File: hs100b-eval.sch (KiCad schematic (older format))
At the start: 42 parts, among them IC1 HS-100B, J1 SPKR, J2 MIC, J3 RADIO_DATA, SW1 MUTE_REC, SW2 MUTE_PLAY, SW3 VOL_DN, SW4 VOL_UP

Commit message: Swap Molex micro USB for CUI
The Molex is nearly impossible to hand solder
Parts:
- removed JP2: USB_A, Connector_USB:USB_Micro-B_Molex_47346-0001, symbol Connector:USB_A
- added JP2: USB_B_Micro, CUI:UJ2-MIBH-4-SMT, symbol Connector:USB_B_Micro
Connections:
- net GND: now also JP2.5 (GND)
- net at L1.1: now also JP2.1 (VBUS)
- net USB-: now reaches C3.1, R1.2
- net USB-: now also JP2.2 (D-)
- net USB+: now reaches C4.1, R2.2
- net USB+: now also JP2.3 (D+)
- net at L2.2: now also JP2.6 (Shield)
- no-connect marks 7 -> 8
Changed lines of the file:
@@
 Sheet 1 1
 Title "HS100B Evaluation Board"
-Date "2021-04-05"
-Rev "1"
+Date "2021-04-14"
+Rev "2"
 Comp "Chris Keller"
 Comment1 ""
@@
 	1    0    0    -1
 $EndComp
-$Comp
-L Connector:USB_A JP2
-U 1 1 6057963A
-P 1350 2850
-F 0 "JP2" H 1407 3317 50  0000 C CNN
-F 1 "USB_A" H 1407 3226 50  0000 C CNN
-F 2 "Connector_USB:USB_Micro-B_Molex_47346-0001" H 1500 2800 50  0001 C CNN
-F 3 "https://www.mouser.com/datasheet/2/276/0473460001_IO_CONNECTORS-229243.pdf" H 1500 2800 50  0001 C CNN
-F 4 "0.95" H 1407 3417 50  0001 C CNN "Price"
-F 5 "538-47346-0001" H 1407 3417 50  0001 C CNN "Vendor Part #"
-F 6 "Mouser" H 1407 3417 50  0001 C CNN "Vendor"
-	1    1350 2850
-	1    0    0    -1
-$EndComp
 Wire Wire Line
 	1350 3250 1350 3600
@@
 NoConn ~ 4050 4150
 NoConn ~ 4050 4350
+$Comp
+L Connector:USB_B_Micro JP2
+U 1 1 6078D129
+P 1350 2850
+F 0 "JP2" H 1407 3317 50  0000 C CNN
+F 1 "USB_B_Micro" H 1407 3226 50  0000 C CNN
+F 2 "CUI:UJ2-MIBH-4-SMT" H 1500 2800 50  0001 C CNN
+F 3 "https://www.mouser.com/datasheet/2/670/uj2_mibh_4_smt-1313358.pdf" H 1500 2800 50  0001 C CNN
+	1    1350 2850
+	1    0    0    -1
+$EndComp
+NoConn ~ 1650 3050
+Text Label 1750 2850 0    50   ~ 0
+USB+
+Text Label 1750 2950 0    50   ~ 0
+USB-
 $EndSCHEMATC

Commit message: Update BOM
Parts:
- IC1: Description LQFP-48 Video-Audio Interface ICs RoHS -> (none); Height 1.6 -> (none); Manufacturer_Name cmedia -> (none); Manufacturer_Part_Number HS-100B -> (none); Price (none) -> 0.78; Vendor (none) -> Symmetry; Vendor Part # (none) -> HS-100B
- JP2: Price (none) -> 0.79; Vendor (none) -> Mouser; Vendor Part # (none) -> 490-UJ2-MIBH-4-SMT
- R4: Vendor Part # 661-RK73Z2ETTD -> 660-RK73Z2ETTD
- R5: Vendor Part # 662-RK73Z2ETTD -> 660-RK73Z2ETTD
- R6: Vendor Part # 663-RK73Z2ETTD -> 660-RK73Z2ETTD

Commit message: Add more test points
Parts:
- added TP1: GND, TestPoint:TestPoint_Pad_D2.0mm, symbol Connector:TestPoint_Flag
- added TP2: 5V, TestPoint:TestPoint_Pad_D1.0mm, symbol Connector:TestPoint_Flag
- C50, C51: footprint 293D477X9010E2TE3:CAPPM7343X430N -> Vishay:CAPPM7343X430N
- TP3: renamed from TP1; value Test_3V3 -> 3V3
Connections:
- net GND: now also TP1.1
- net VBUS: now also TP2.1
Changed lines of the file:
@@
 $EndComp
 $Comp
-L Connector:TestPoint_Flag TP1
+L Connector:TestPoint_Flag TP3
 U 1 1 605AD28D
 P 3450 4250
-F 0 "TP1" V 3847 4298 50  0000 C CNN
-F 1 "Test_3V3" V 3756 4298 50  0000 C CNN
+F 0 "TP3" V 3847 4298 50  0000 C CNN
+F 1 "3V3" V 3756 4298 50  0000 C CNN
 F 2 "TestPoint:TestPoint_Pad_D1.0mm" H 3650 4250 50  0001 C CNN
 F 3 "-" H 3650 4250 50  0001 C CNN
@@
 F 0 "C50" V 6855 3950 50  0000 C CNN
 F 1 "470μF" V 6764 3950 50  0000 C CNN
-F 2 "293D477X9010E2TE3:CAPPM7343X430N" H 6638 3800 50  0001 C CNN
+F 2 "Vishay:CAPPM7343X430N" H 6638 3800 50  0001 C CNN
 F 3 "https://www.mouser.com/datasheet/2/427/293d-1763499.pdf" H 6600 3950 50  0001 C CNN
 F 4 "1.3" H 6855 4050 50  0001 C CNN "Price"
@@
 F 0 "C51" V 7150 4050 50  0000 C CNN
 F 1 "470μF" V 7050 4050 50  0000 C CNN
-F 2 "293D477X9010E2TE3:CAPPM7343X430N" H 6938 3900 50  0001 C CNN
+F 2 "Vishay:CAPPM7343X430N" H 6938 3900 50  0001 C CNN
 F 3 "https://www.mouser.com/datasheet/2/427/293d-1763499.pdf" H 6900 4050 50  0001 C CNN
 F 4 "1.3" H 7150 4150 50  0001 C CNN "Price"
@@
 	2050 2650 2150 2650
 Wire Wire Line
-	2150 2650 2150 2400
+	2150 2650 2150 2500
 Wire Wire Line
 	8900 5150 8700 5150
@@
 	2750 5300 2750 5800
 Wire Wire Line
-	1350 3250 1350 3600
+	1350 3250 1350 3550
 Wire Wire Line
 	1250 3250 1250 3300
@@
 	5050 5450 5150 5450
 Wire Wire Line
-	4950 5450 4950 5650
+	4950 5450 4950 5600
 Wire Wire Line
 	5750 4450 7000 4450
@@
 	6100 5100 6100 3700
 Wire Wire Line
-	7200 2300 7200 2600
+	7200 2300 7200 2450
 Wire Wire Line
 	5900 2600 5900 3400
@@
 NoConn ~ 4050 4350
 NoConn ~ 1650 3050
+$Comp
+L Connector:TestPoint_Flag TP2
+U 1 1 607D02CD
+P 7200 2450
+F 0 "TP2" V 7354 2590 50  0000 L CNN
+F 1 "5V" V 7263 2590 50  0000 L CNN
+F 2 "TestPoint:TestPoint_Pad_D1.0mm" H 7400 2450 50  0001 C CNN
+F 3 "-" H 7400 2450 50  0001 C CNN
+F 4 "0" H 7597 2598 50  0001 C CNN "Price"
+F 5 "-" H 7597 2598 50  0001 C CNN "Vendor Part #"
+F 6 "-" H 7597 2598 50  0001 C CNN "Vendor"
+	1    7200 2450
+	0    -1   -1   0
+$EndComp
+Connection ~ 2150 2500
+Wire Wire Line
+	2150 2500 2150 2400
+$Comp
+L Connector:TestPoint_Flag TP1
+U 1 1 607D1285
+P 4950 5600
+F 0 "TP1" H 5210 5694 50  0000 L CNN
+F 1 "GND" H 5210 5603 50  0000 L CNN
+F 2 "TestPoint:TestPoint_Pad_D2.0mm" H 5150 5600 50  0001 C CNN
+F 3 "-" H 5150 5600 50  0001 C CNN
+F 4 "0" H 5347 5748 50  0001 C CNN "Price"
+F 5 "-" H 5347 5748 50  0001 C CNN "Vendor Part #"
+F 6 "-" H 5347 5748 50  0001 C CNN "Vendor"
+	1    4950 5600
+	1    0    0    -1
+$EndComp
+Connection ~ 1350 3550
+Wire Wire Line
+	1350 3550 1350 3600
+Connection ~ 4950 5600
+Wire Wire Line
+	4950 5600 4950 5650
+Connection ~ 7200 2550
+Wire Wire Line
+	7200 2550 7200 2600
+Connection ~ 7200 2450
+Wire Wire Line
+	7200 2450 7200 2550
 $EndSCHEMATC

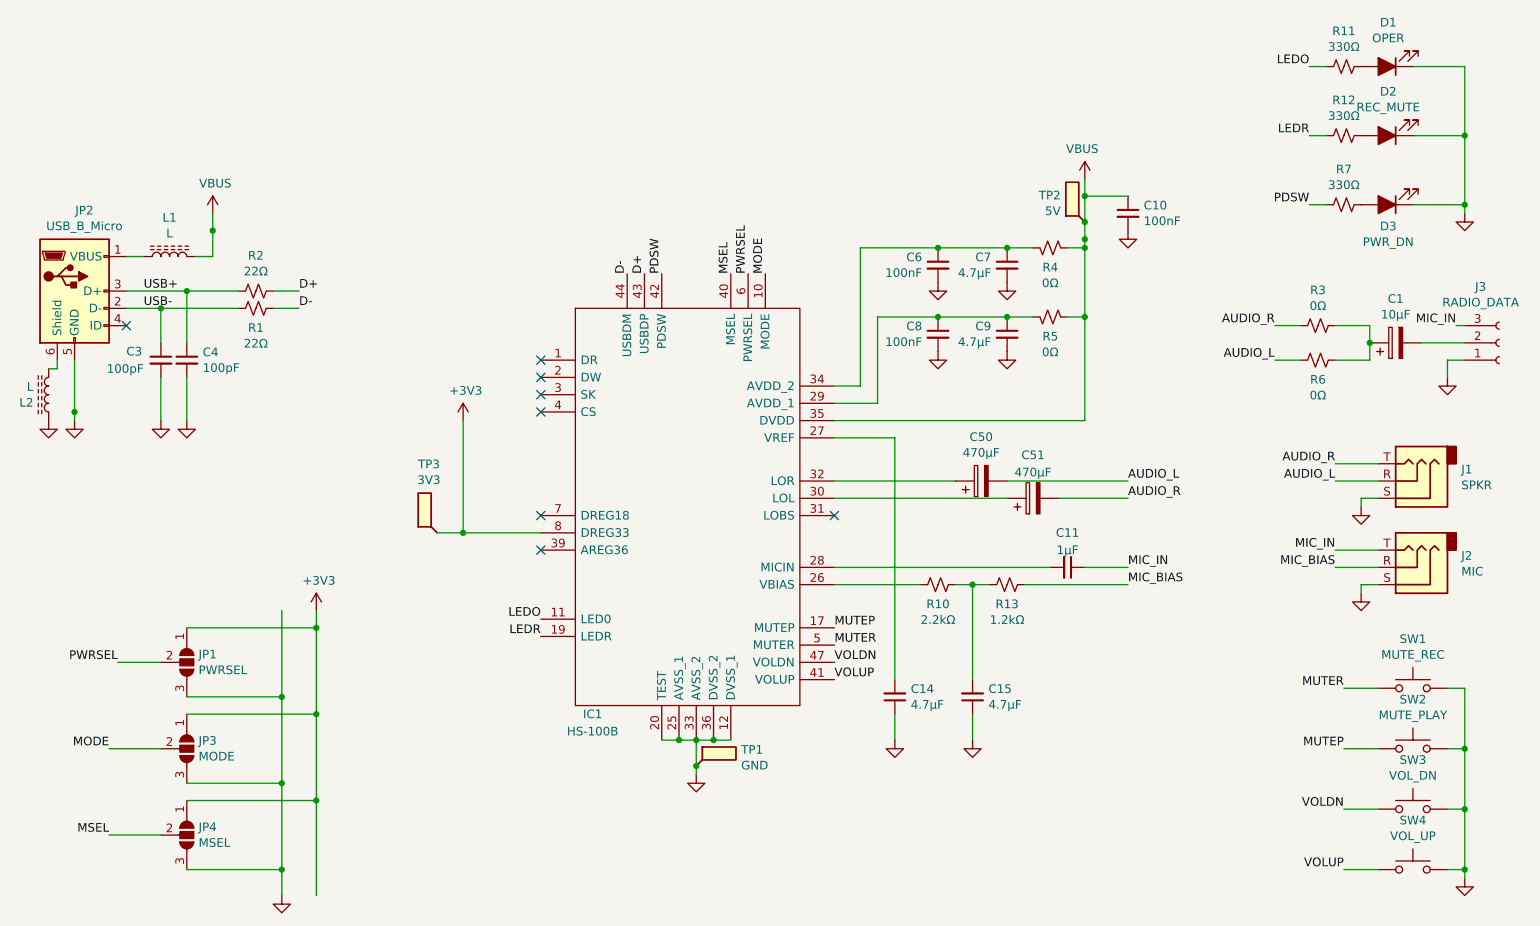
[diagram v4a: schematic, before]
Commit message: Move 5V test point to directly off USB
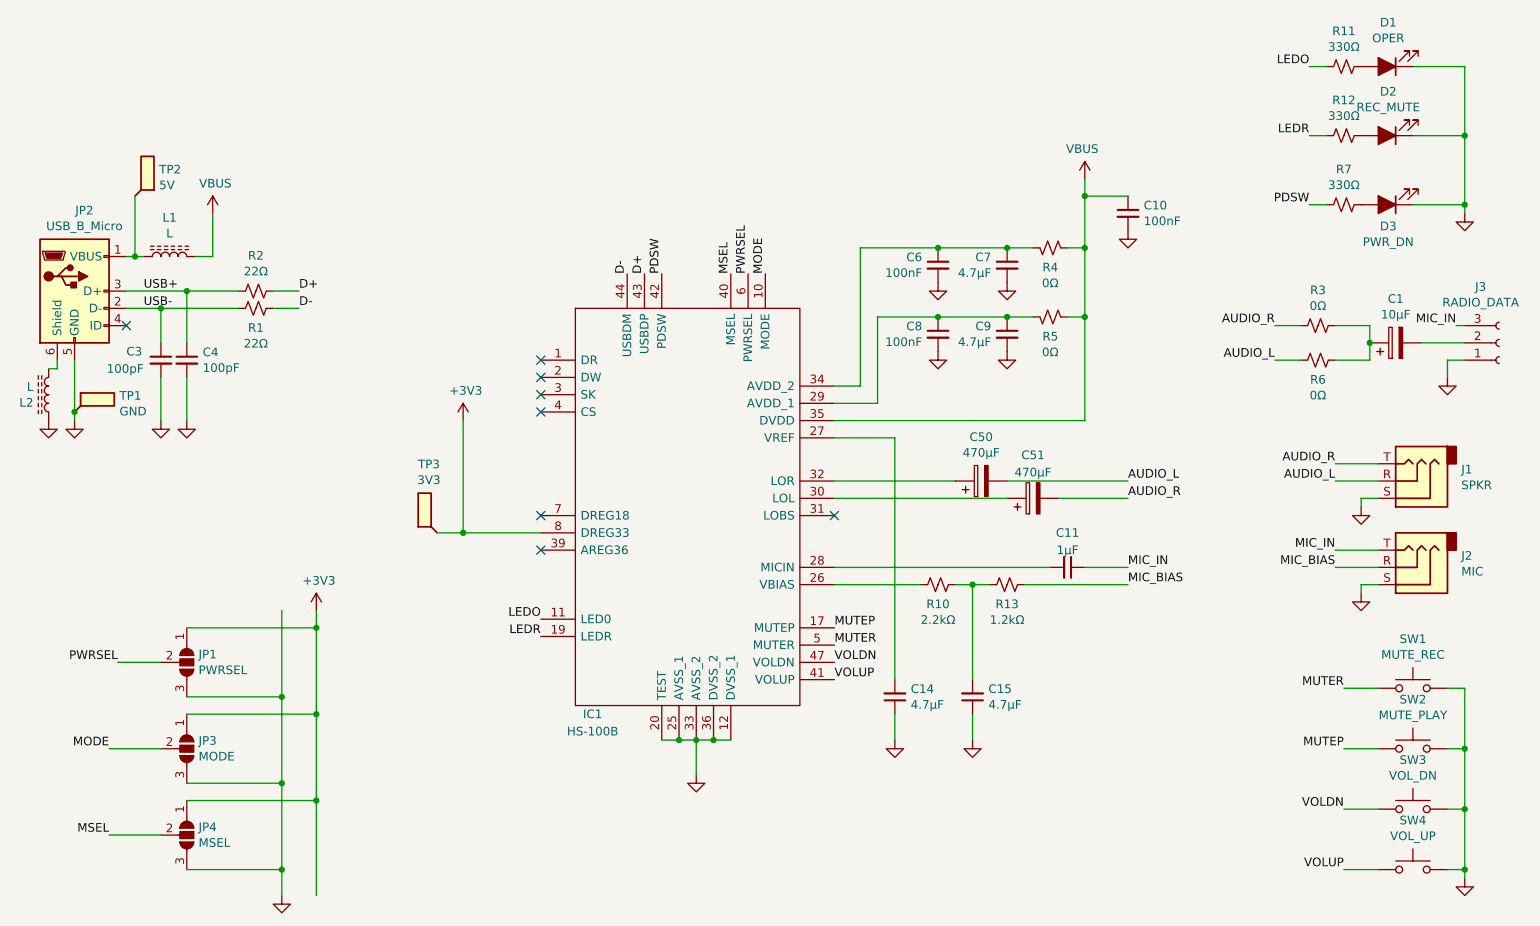
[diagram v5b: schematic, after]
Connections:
- net VBUS: no longer TP2.1
- net at JP2.1 (VBUS), L1.1: now also TP2.1
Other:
- moved on the sheet: TP1, TP2
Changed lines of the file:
@@
 	2500 2950 2650 2950
 Wire Wire Line
-	1650 2650 1750 2650
+	1650 2650 1700 2650
 Wire Wire Line
 	1850 3150 1850 2950
@@
 	2050 2650 2150 2650
 Wire Wire Line
-	2150 2650 2150 2500
-Wire Wire Line
 	8900 5150 8700 5150
 Wire Wire Line
@@
 	2750 5300 2750 5800
 Wire Wire Line
-	1350 3250 1350 3550
-Wire Wire Line
 	1250 3250 1250 3300
 Wire Wire Line
@@
 	5050 5450 5150 5450
 Wire Wire Line
-	4950 5450 4950 5600
-Wire Wire Line
 	5750 4450 7000 4450
 Wire Wire Line
@@
 Wire Wire Line
 	6100 5100 6100 3700
-Wire Wire Line
-	7200 2300 7200 2450
 Wire Wire Line
 	5900 2600 5900 3400
@@
 L Connector:TestPoint_Flag TP2
 U 1 1 607D02CD
-P 7200 2450
-F 0 "TP2" V 7354 2590 50  0000 L CNN
-F 1 "5V" V 7263 2590 50  0000 L CNN
-F 2 "TestPoint:TestPoint_Pad_D1.0mm" H 7400 2450 50  0001 C CNN
-F 3 "-" H 7400 2450 50  0001 C CNN
-F 4 "0" H 7597 2598 50  0001 C CNN "Price"
-F 5 "-" H 7597 2598 50  0001 C CNN "Vendor Part #"
-F 6 "-" H 7597 2598 50  0001 C CNN "Vendor"
-	1    7200 2450
-	0    -1   -1   0
+P 1700 2300
+F 0 "TP2" V 1854 2440 50  0000 L CNN
+F 1 "5V" V 1763 2440 50  0000 L CNN
+F 2 "TestPoint:TestPoint_Pad_D1.0mm" H 1900 2300 50  0001 C CNN
+F 3 "-" H 1900 2300 50  0001 C CNN
+F 4 "0" H 2097 2448 50  0001 C CNN "Price"
+F 5 "-" H 2097 2448 50  0001 C CNN "Vendor Part #"
+F 6 "-" H 2097 2448 50  0001 C CNN "Vendor"
+	1    1700 2300
+	0    1    -1   0
 $EndComp
-Connection ~ 2150 2500
-Wire Wire Line
-	2150 2500 2150 2400
 $Comp
 L Connector:TestPoint_Flag TP1
 U 1 1 607D1285
-P 4950 5600
-F 0 "TP1" H 5210 5694 50  0000 L CNN
-F 1 "GND" H 5210 5603 50  0000 L CNN
-F 2 "TestPoint:TestPoint_Pad_D2.0mm" H 5150 5600 50  0001 C CNN
-F 3 "-" H 5150 5600 50  0001 C CNN
-F 4 "0" H 5347 5748 50  0001 C CNN "Price"
-F 5 "-" H 5347 5748 50  0001 C CNN "Vendor Part #"
-F 6 "-" H 5347 5748 50  0001 C CNN "Vendor"
-	1    4950 5600
+P 1350 3550
+F 0 "TP1" H 1610 3644 50  0000 L CNN
+F 1 "GND" H 1610 3553 50  0000 L CNN
+F 2 "TestPoint:TestPoint_Pad_D2.0mm" H 1550 3550 50  0001 C CNN
+F 3 "-" H 1550 3550 50  0001 C CNN
+F 4 "0" H 1747 3698 50  0001 C CNN "Price"
+F 5 "-" H 1747 3698 50  0001 C CNN "Vendor Part #"
+F 6 "-" H 1747 3698 50  0001 C CNN "Vendor"
+	1    1350 3550
 	1    0    0    -1
 $EndComp
+Wire Wire Line
+	2150 2400 2150 2650
+Wire Wire Line
+	1350 3250 1350 3550
 Connection ~ 1350 3550
 Wire Wire Line
 	1350 3550 1350 3600
-Connection ~ 4950 5600
-Wire Wire Line
-	4950 5600 4950 5650
-Connection ~ 7200 2550
-Wire Wire Line
-	7200 2550 7200 2600
-Connection ~ 7200 2450
-Wire Wire Line
-	7200 2450 7200 2550
+Wire Wire Line
+	1700 2300 1700 2650
+Wire Wire Line
+	4950 5450 4950 5650
+Wire Wire Line
+	7200 2300 7200 2600
+Connection ~ 1700 2650
+Wire Wire Line
+	1700 2650 1750 2650
 $EndSCHEMATC

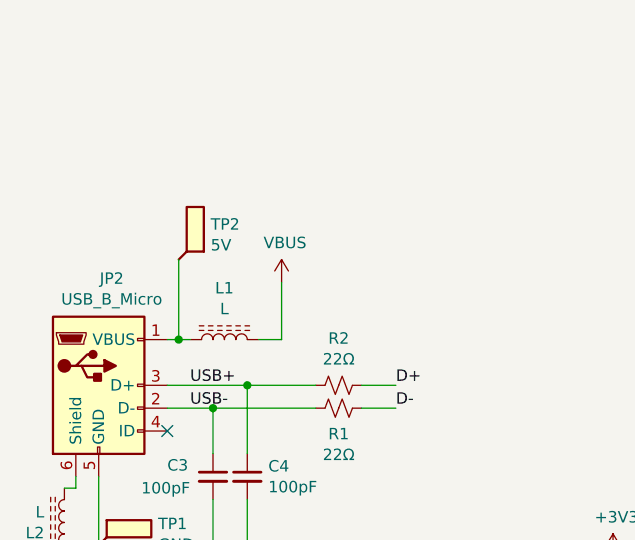
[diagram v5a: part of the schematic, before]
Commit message: Incorporate learnings from first physical prototype
* Button footprint pad numberings are wrong for symbol, so they were always pressed
* Turn J3 for solderability
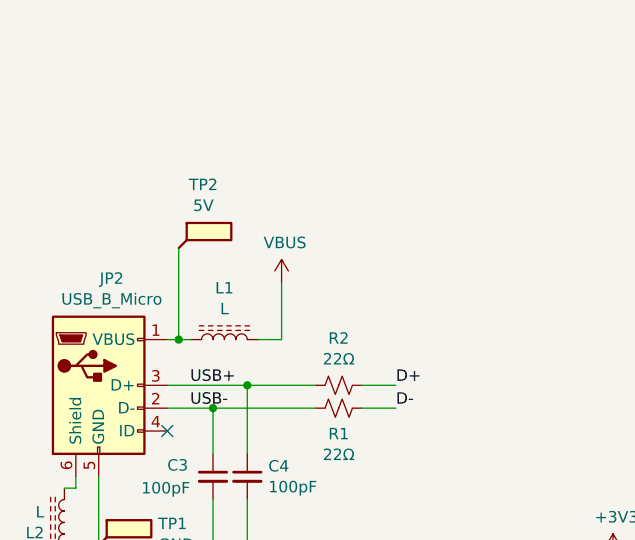
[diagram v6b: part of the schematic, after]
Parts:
- SW1, SW2, SW3, SW4: footprint Button_Switch_SMD:SW_SPST_Omron_B3FS-100xP -> Omron:SW_SPST_Omron_B3FS-100xP
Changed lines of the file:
@@
 Sheet 1 1
 Title "HS100B Evaluation Board"
-Date "2021-04-14"
+Date "2021-04-18"
 Rev "2"
 Comp "Chris Keller"
@@
 F 0 "SW1" H 9100 5435 50  0000 C CNN
 F 1 "MUTE_REC" H 9100 5344 50  0000 C CNN
-F 2 "Button_Switch_SMD:SW_SPST_Omron_B3FS-100xP" H 9100 5350 50  0001 C CNN
+F 2 "Omron:SW_SPST_Omron_B3FS-100xP" H 9100 5350 50  0001 C CNN
 F 3 "https://www.mouser.com/datasheet/2/307/omron_B3FS-1189765.pdf" H 9100 5350 50  0001 C CNN
 F 4 "0.58" H 9100 5535 50  0001 C CNN "Price"
@@
 F 0 "SW2" H 9100 5785 50  0000 C CNN
 F 1 "MUTE_PLAY" H 9100 5694 50  0000 C CNN
-F 2 "Button_Switch_SMD:SW_SPST_Omron_B3FS-100xP" H 9100 5700 50  0001 C CNN
+F 2 "Omron:SW_SPST_Omron_B3FS-100xP" H 9100 5700 50  0001 C CNN
 F 3 "https://www.mouser.com/datasheet/2/307/omron_B3FS-1189765.pdf" H 9100 5700 50  0001 C CNN
 F 4 "0.58" H 9100 5885 50  0001 C CNN "Price"
@@
 F 0 "SW3" H 9100 6135 50  0000 C CNN
 F 1 "VOL_DN" H 9100 6044 50  0000 C CNN
-F 2 "Button_Switch_SMD:SW_SPST_Omron_B3FS-100xP" H 9100 6050 50  0001 C CNN
+F 2 "Omron:SW_SPST_Omron_B3FS-100xP" H 9100 6050 50  0001 C CNN
 F 3 "https://www.mouser.com/datasheet/2/307/omron_B3FS-1189765.pdf" H 9100 6050 50  0001 C CNN
 F 4 "0.58" H 9100 6235 50  0001 C CNN "Price"
@@
 F 0 "SW4" H 9100 6485 50  0000 C CNN
 F 1 "VOL_UP" H 9100 6394 50  0000 C CNN
-F 2 "Button_Switch_SMD:SW_SPST_Omron_B3FS-100xP" H 9100 6400 50  0001 C CNN
+F 2 "Omron:SW_SPST_Omron_B3FS-100xP" H 9100 6400 50  0001 C CNN
 F 3 "https://www.mouser.com/datasheet/2/307/omron_B3FS-1189765.pdf" H 9100 6400 50  0001 C CNN
 F 4 "0.58" H 9100 6585 50  0001 C CNN "Price"
@@
 	2050 2650 2150 2650
 Wire Wire Line
+	2150 2650 2150 2400
+Wire Wire Line
 	8900 5150 8700 5150
 Wire Wire Line
@@
 	2750 5300 2750 5800
 Wire Wire Line
+	1350 3250 1350 3550
+Wire Wire Line
 	1250 3250 1250 3300
 Wire Wire Line
@@
 	5050 5450 5150 5450
 Wire Wire Line
+	4950 5450 4950 5650
+Wire Wire Line
 	5750 4450 7000 4450
 Wire Wire Line
@@
 Wire Wire Line
 	6100 5100 6100 3700
+Wire Wire Line
+	7200 2300 7200 2600
 Wire Wire Line
 	5900 2600 5900 3400
@@
 $Comp
 L Connector:TestPoint_Flag TP2
-U 1 1 607D02CD
-P 1700 2300
-F 0 "TP2" V 1854 2440 50  0000 L CNN
-F 1 "5V" V 1763 2440 50  0000 L CNN
-F 2 "TestPoint:TestPoint_Pad_D1.0mm" H 1900 2300 50  0001 C CNN
-F 3 "-" H 1900 2300 50  0001 C CNN
-F 4 "0" H 2097 2448 50  0001 C CNN "Price"
-F 5 "-" H 2097 2448 50  0001 C CNN "Vendor Part #"
-F 6 "-" H 2097 2448 50  0001 C CNN "Vendor"
-	1    1700 2300
-	0    1    -1   0
-$EndComp
+U 1 1 607D2415
+P 1700 2250
+F 0 "TP2" H 1808 2527 50  0000 C CNN
+F 1 "5V" H 1808 2436 50  0000 C CNN
+F 2 "TestPoint:TestPoint_Pad_D1.0mm" H 1900 2250 50  0001 C CNN
+F 3 "-" H 1900 2250 50  0001 C CNN
+F 4 "0" H 2097 2398 50  0001 C CNN "Price"
+F 5 "-" H 2097 2398 50  0001 C CNN "Vendor Part #"
+F 6 "-" H 2097 2398 50  0001 C CNN "Vendor"
+	1    1700 2250
+	1    0    0    -1
+$EndComp
+Wire Wire Line
+	1700 2250 1700 2650
+Connection ~ 1700 2650
+Wire Wire Line
+	1700 2650 1750 2650
 $Comp
 L Connector:TestPoint_Flag TP1
-U 1 1 607D1285
+U 1 1 607DDFB1
 P 1350 3550
 F 0 "TP1" H 1610 3644 50  0000 L CNN
@@
 	1    0    0    -1
 $EndComp
-Wire Wire Line
-	2150 2400 2150 2650
-Wire Wire Line
-	1350 3250 1350 3550
 Connection ~ 1350 3550
 Wire Wire Line
 	1350 3550 1350 3600
-Wire Wire Line
-	1700 2300 1700 2650
-Wire Wire Line
-	4950 5450 4950 5650
-Wire Wire Line
-	7200 2300 7200 2600
-Connection ~ 1700 2650
-Wire Wire Line
-	1700 2650 1750 2650
 $EndSCHEMATC

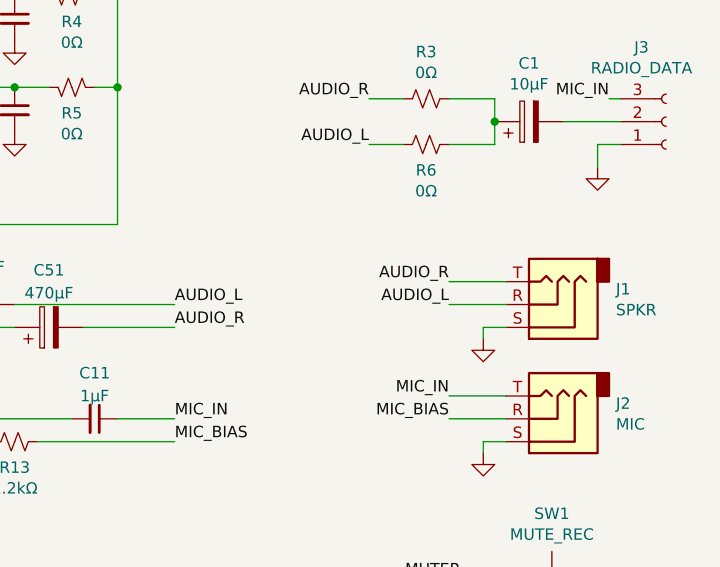
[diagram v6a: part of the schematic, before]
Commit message: Fix R and L on J1
Resolves #1
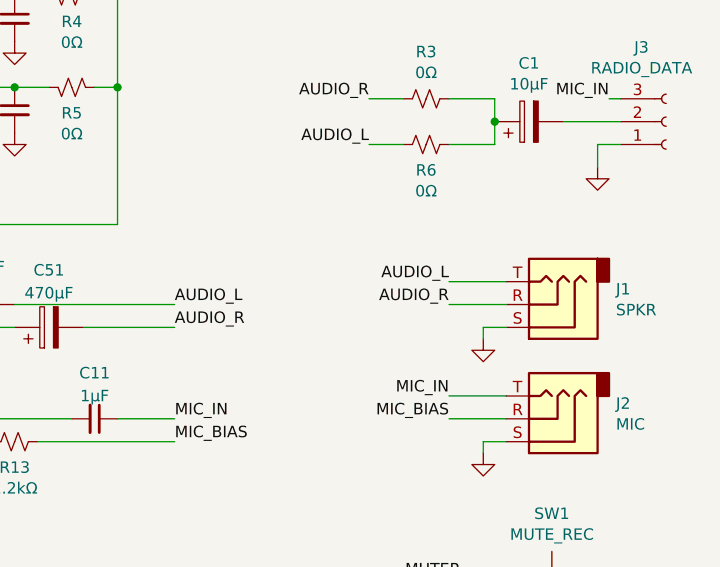
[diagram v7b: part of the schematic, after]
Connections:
- net AUDIO_L: now also J1.T; no longer J1.R
- net AUDIO_R: now also J1.R; no longer J1.T
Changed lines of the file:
@@
 Sheet 1 1
 Title "HS100B Evaluation Board"
-Date "2021-04-18"
-Rev "2"
+Date "2021-04-21"
+Rev "3"
 Comp "Chris Keller"
 Comment1 "Licensed under Creative Commons CC-BY-4.0"
@@
 Text Label 8650 4450 2    50   ~ 0
 MIC_BIAS
+Text Label 8650 3850 2    50   ~ 0
+AUDIO_L
 Text Label 8650 3950 2    50   ~ 0
-AUDIO_L
-Text Label 8650 3850 2    50   ~ 0
 AUDIO_R
 Text Label 9350 3050 2    50   ~ 0
